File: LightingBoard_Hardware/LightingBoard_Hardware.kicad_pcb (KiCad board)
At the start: 2 copper layers, 61 x 108.8 mm, 19 parts, among them U1 LDD-1500L, U2 LDD-1500L, U3 TM4C129E_Launchpad, U4 +5V OKI

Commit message: Fixed detached ground polygon
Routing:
- net GND: track 8.38 -> 17.5 mm, vias 2 -> 4
- net Headlight_OnOff_PWM1: track 111.4 -> 110.1 mm
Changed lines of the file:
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@@
     (thickness 1.6)
     (drawings 29)
-    (tracks 81)
+    (tracks 88)
     (zones 0)
     (modules 19)
@@
   )
   (setup
-    (last_trace_width 0.25)
+    (last_trace_width 1.27)
     (user_trace_width 0.0381)
     (user_trace_width 0.03998)
@@
   (segment (start 158.496 83.439) (end 155.956 83.439) (width 1.27) (layer F.Cu) (net 2))
   (segment (start 158.496 61.849) (end 155.956 61.849) (width 1.27) (layer F.Cu) (net 2))
+  (segment (start 155.956 61.849) (end 151.384 61.849) (width 1.27) (layer B.Cu) (net 2))
+  (segment (start 155.956 83.439) (end 151.384 83.439) (width 1.27) (layer B.Cu) (net 2))
+  (segment (start 151.384 61.849) (end 151.384 61.849) (width 1.27) (layer B.Cu) (net 2))
+  (via (at 151.384 61.849) (size 1.27) (drill 0.4) (layers F.Cu B.Cu) (net 2))
+  (segment (start 151.384 83.439) (end 151.384 83.439) (width 1.27) (layer B.Cu) (net 2))
+  (via (at 151.384 83.439) (size 1.27) (drill 0.4) (layers F.Cu B.Cu) (net 2))
   (segment (start 138.303 123.317) (end 138.303 119.634) (width 0.381) (layer F.Cu) (net 3))
   (segment (start 120.2944 112.775) (end 135.763 112.775) (width 0.762) (layer F.Cu) (net 3))
@@
   (segment (start 121.031 51.943) (end 121.031 47.879) (width 0.381) (layer B.Cu) (net 13))
   (segment (start 153.67 97.536) (end 153.67 97.536) (width 0.25) (layer F.Cu) (net 14))
-  (segment (start 151.416 80.296) (end 151.416 98.679) (width 0.381) (layer B.Cu) (net 14))
-  (segment (start 150.114 78.994) (end 151.416 80.296) (width 0.381) (layer B.Cu) (net 14))
-  (segment (start 121.7047 78.994) (end 150.114 78.994) (width 0.381) (layer B.Cu) (net 14))
   (segment (start 118.008001 74.903601) (end 118.008001 75.297301) (width 0.381) (layer B.Cu) (net 14))
   (segment (start 118.008001 75.297301) (end 121.7047 78.994) (width 0.381) (layer B.Cu) (net 14))
@@
   (segment (start 154.714 43.561) (end 153.67 44.605) (width 0.381) (layer F.Cu) (net 14))
   (segment (start 153.67 45.170685) (end 153.67 97.536) (width 0.381) (layer F.Cu) (net 14))
+  (segment (start 151.416 98.679) (end 149.225 96.488) (width 0.381) (layer B.Cu) (net 14))
+  (segment (start 149.225 96.488) (end 149.225 80.264) (width 0.381) (layer B.Cu) (net 14))
+  (segment (start 149.225 80.264) (end 147.955 78.994) (width 0.381) (layer B.Cu) (net 14))
+  (segment (start 147.955 78.994) (end 121.7047 78.994) (width 0.381) (layer B.Cu) (net 14))
   (segment (start 115.468001 74.903601) (end 115.468001 75.297301) (width 0.381) (layer B.Cu) (net 15))
   (segment (start 149.257 74.93) (end 151.416 77.089) (width 0.381) (layer B.Cu) (net 15))

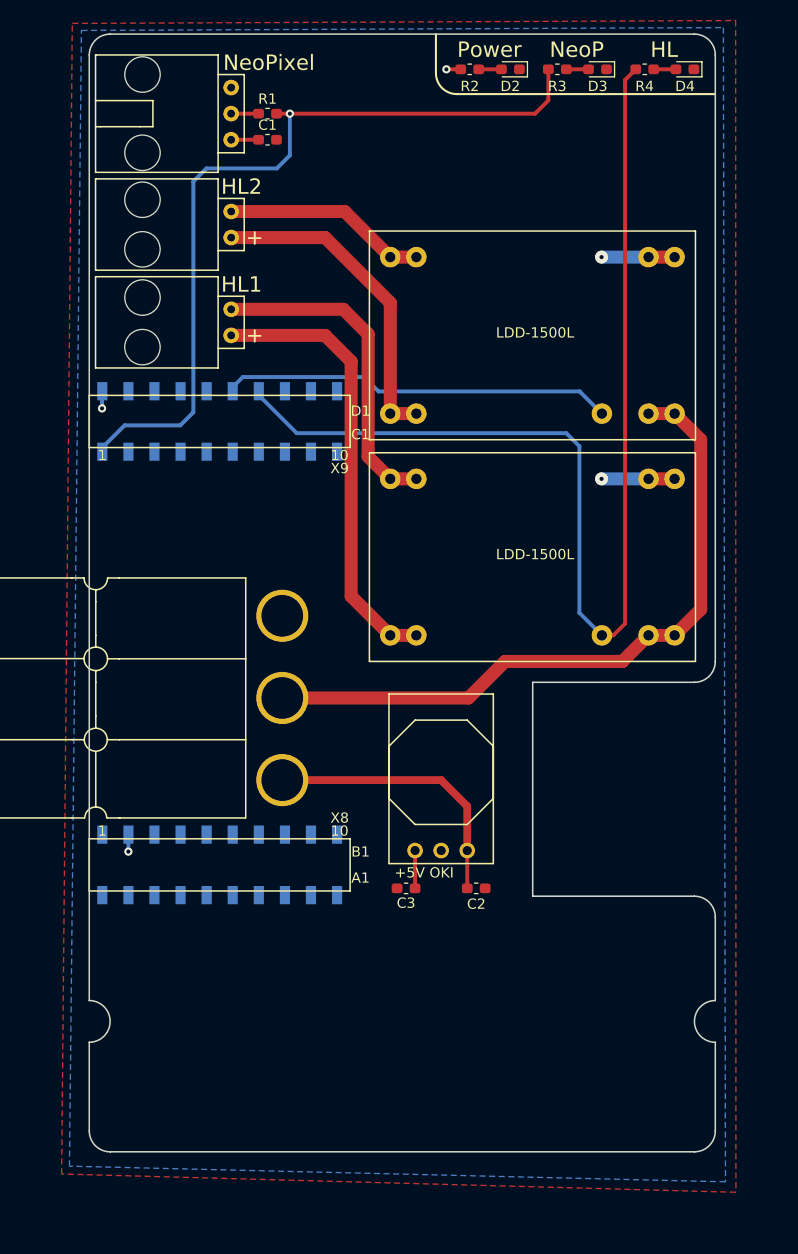
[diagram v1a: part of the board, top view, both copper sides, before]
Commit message: Traces probably finished
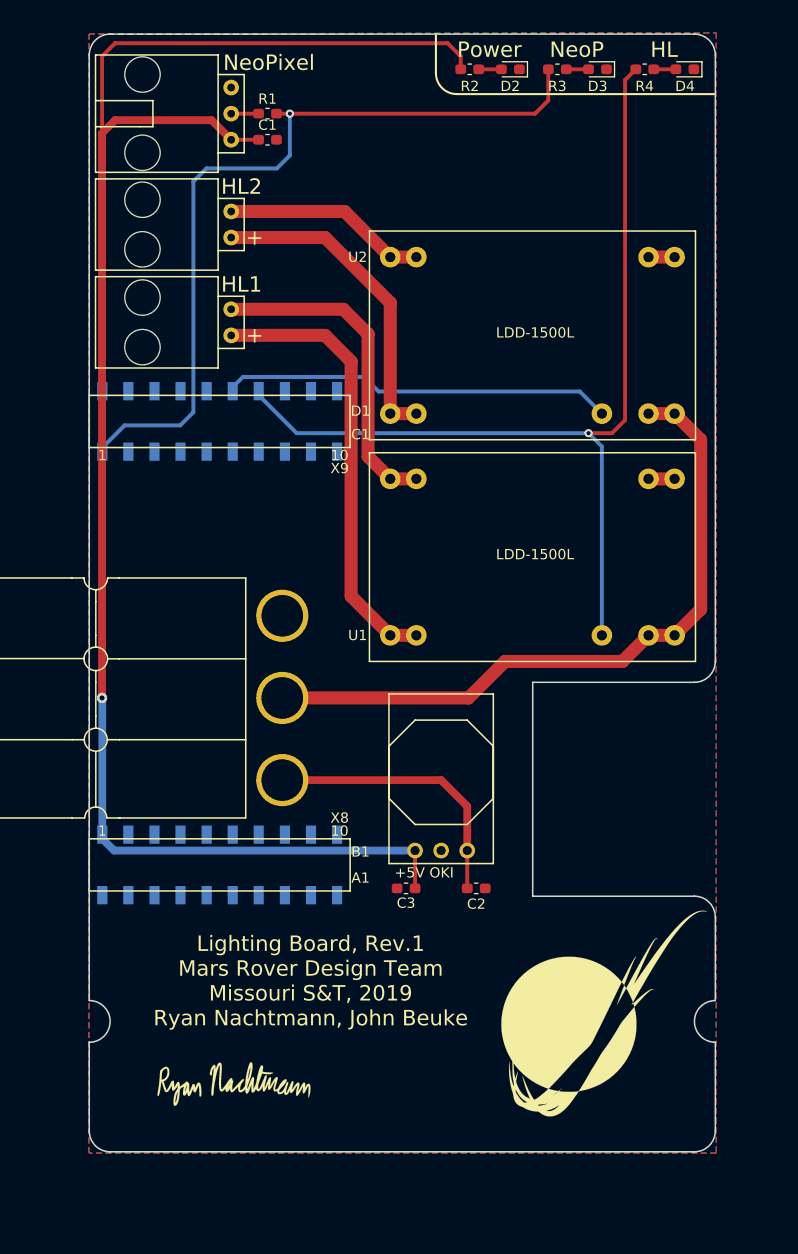
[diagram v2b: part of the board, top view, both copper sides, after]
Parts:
- added G***: LOGO, LightingBoard_Hardware2:Ryan Signature, F.Cu at (116.2, 142.7)
- added G***: LOGO, MRDT_Silkscreens:MRDT_Logo_20mm, F.Cu at (151.6, 135.5)
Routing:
- net +5V: track 7.75 -> 164.6 mm
- net Headlight_OnOff_PWM1: track 110.1 -> 92.9 mm, vias 0 -> 1
- net GND: track 17.5 -> 5.08 mm, vias 4 -> 0
- added copper zone on B.Cu, net GND
- removed copper zone on B.Cu, net +5V
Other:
- board text added: "Lighting Board, Rev.1 Mars Rover Design Team Missouri S&T, 2019 Ryan Nachtmann, John Beuke"

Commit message: Probably finished the traces 2.0
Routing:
- net +5V: vias 1 -> 2
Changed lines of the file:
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@@
     (thickness 1.6)
     (drawings 30)
-    (tracks 89)
+    (tracks 91)
     (zones 0)
     (modules 21)
@@
   )
   (setup
-    (last_trace_width 0.25)
+    (last_trace_width 0.762)
     (user_trace_width 0.0381)
     (user_trace_width 0.03998)
@@
   (segment (start 102.768001 104.800001) (end 102.743 104.775) (width 0.762) (layer B.Cu) (net 1))
   (segment (start 102.743 104.775) (end 102.743 49.784) (width 0.762) (layer F.Cu) (net 1))
-  (segment (start 102.743 49.784) (end 104.013 48.514) (width 0.762) (layer F.Cu) (net 1))
-  (segment (start 104.013 48.514) (end 104.013 48.514) (width 0.762) (layer F.Cu) (net 1))
-  (segment (start 115.316 50.419) (end 113.411 48.514) (width 0.762) (layer F.Cu) (net 1))
-  (segment (start 113.411 48.514) (end 104.013 48.514) (width 0.762) (layer F.Cu) (net 1))
   (segment (start 102.743 49.784) (end 102.743 42.291) (width 0.381) (layer F.Cu) (net 1))
   (segment (start 102.743 42.291) (end 104.013 41.021) (width 0.381) (layer F.Cu) (net 1))
@@
   (segment (start 136.398 41.021) (end 137.668 42.291) (width 0.381) (layer F.Cu) (net 1))
   (segment (start 137.668 42.291) (end 137.668 43.561) (width 0.381) (layer F.Cu) (net 1))
+  (segment (start 102.743 49.784) (end 102.743 49.784) (width 0.762) (layer F.Cu) (net 1))
+  (via (at 102.743 49.784) (size 1) (drill 0.5) (layers F.Cu B.Cu) (net 1))
+  (segment (start 102.743 49.784) (end 104.013 48.514) (width 0.762) (layer B.Cu) (net 1))
+  (segment (start 115.316 50.419) (end 113.411 48.514) (width 0.762) (layer B.Cu) (net 1))
+  (segment (start 113.411 48.514) (end 104.013 48.514) (width 0.762) (layer B.Cu) (net 1))
   (segment (start 158.496 83.439) (end 155.956 83.439) (width 1.27) (layer F.Cu) (net 2))
   (segment (start 158.496 61.849) (end 155.956 61.849) (width 1.27) (layer F.Cu) (net 2))
@@
   (segment (start 153.67 44.605) (end 153.67 44.605) (width 0.25) (layer F.Cu) (net 14))
   (segment (start 154.714 43.561) (end 153.67 44.605) (width 0.381) (layer F.Cu) (net 14))
-  (segment (start 151.416 98.679) (end 151.416 80.296) (width 0.381) (layer B.Cu) (net 14))
-  (segment (start 151.416 80.296) (end 150.114 78.994) (width 0.381) (layer B.Cu) (net 14))
   (segment (start 150.114 78.994) (end 121.7047 78.994) (width 0.381) (layer B.Cu) (net 14))
   (segment (start 151.416 80.296) (end 151.416 80.296) (width 0.381) (layer B.Cu) (net 14))
   (segment (start 150.114 78.994) (end 150.114 78.994) (width 0.381) (layer B.Cu) (net 14))
-  (via (at 150.114 78.994) (size 0.8) (drill 0.4) (layers F.Cu B.Cu) (net 14))
-  (segment (start 150.114 78.994) (end 152.4 78.994) (width 0.381) (layer F.Cu) (net 14))
-  (segment (start 152.4 78.994) (end 153.67 77.724) (width 0.381) (layer F.Cu) (net 14))
-  (segment (start 153.67 77.724) (end 153.67 44.605) (width 0.381) (layer F.Cu) (net 14))
+  (segment (start 153.67 44.605) (end 153.67 44.605) (width 0.25) (layer F.Cu) (net 14))
+  (via (at 153.67 44.605) (size 0.8) (drill 0.4) (layers F.Cu B.Cu) (net 14))
+  (segment (start 153.67 44.605) (end 153.67 77.724) (width 0.381) (layer B.Cu) (net 14))
+  (segment (start 153.67 77.724) (end 152.4 78.994) (width 0.381) (layer B.Cu) (net 14))
+  (segment (start 152.4 78.994) (end 150.114 78.994) (width 0.381) (layer B.Cu) (net 14))
+  (segment (start 151.416 98.679) (end 151.416 80.296) (width 0.381) (layer B.Cu) (net 14))
+  (segment (start 151.416 80.296) (end 150.114 78.994) (width 0.381) (layer B.Cu) (net 14))
   (segment (start 115.468001 74.903601) (end 115.468001 75.297301) (width 0.381) (layer B.Cu) (net 15))
   (segment (start 149.257 74.93) (end 151.416 77.089) (width 0.381) (layer B.Cu) (net 15))

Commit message: Added John's Signature
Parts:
- added G***: LOGO, LightingBoard_Hardware2:John Signature, F.Cu at (133.6, 143.3)

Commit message: Final Board
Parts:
- moved Conn2 0.64 mm to (114.7, 68.2)
- moved Conn3 0.64 mm to (114.7, 58.7)
- moved Conn4 0.64 mm to (114.7, 47.9)
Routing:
- net /Headlight_V2-: track 19.9 -> 23.8 mm
- net /Headlight_V2+: track 31.5 -> 33.6 mm
- net /Headlight_V1+: track 43.5 -> 44.6 mm
- net /Headlight_V1-: track 31.9 -> 32.9 mm
- net Net-(Conn4-Pad2): track 2.67 -> 3.30 mm
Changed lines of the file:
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@@
     (thickness 1.6)
     (drawings 30)
-    (tracks 91)
+    (tracks 99)
     (zones 0)
     (modules 22)
@@
   )
   (setup
-    (last_trace_width 0.25)
+    (last_trace_width 1.905)
     (user_trace_width 0.0381)
     (user_trace_width 0.03998)
@@
     (user_trace_width 0.762)
     (user_trace_width 1.27)
+    (user_trace_width 1.905)
     (trace_clearance 0.2)
     (zone_clearance 0.508)
@@
     (solder_mask_min_width 0.25)
     (aux_axis_origin 0 0)
-    (visible_elements 7FFFFFFF)
+    (visible_elements 7FFFEFFF)
     (pcbplotparams
       (layerselection 0x010fc_ffffffff)
@@
   )
   (module MRDT_Connectors:MOLEX_SL_02_Horizontal (layer F.Cu)
-    (at 115.316 68.199 90)
+    (at 114.681 68.199 90)
     (fp_text reference Conn2 (at 0 2.54 90) (layer F.SilkS) hide
       (effects (font (size 1 1) (thickness 0.15)))
@@
   )
   (module MRDT_Connectors:MOLEX_SL_02_Horizontal (layer F.Cu)
-    (at 115.316 58.674 90)
+    (at 114.681 58.674 90)
     (fp_text reference Conn3 (at 0 2.54 90) (layer F.SilkS) hide
       (effects (font (size 1 1) (thickness 0.15)))
@@
   )
   (module MRDT_Connectors:MOLEX_SL_03_Horizontal (layer F.Cu)
-    (at 115.316 47.879 90)
+    (at 114.681 47.879 90)
     (fp_text reference Conn4 (at -1.27 2.54 90) (layer F.SilkS) hide
       (effects (font (size 1 1) (thickness 0.15)))
@@
   (gr_arc (start 101.4984 136.271) (end 101.4984 138.303) (angle -180) (layer Edge.Cuts) (width 0.15))
   (segment (start 133.223 119.634) (end 133.223 123.317) (width 0.381) (layer F.Cu) (net 1))
-  (segment (start 117.983 50.419) (end 115.316 50.419) (width 0.381) (layer F.Cu) (net 1))
   (segment (start 102.768001 118.477301) (end 102.768001 118.083601) (width 0.762) (layer B.Cu) (net 1))
   (segment (start 102.768001 118.477301) (end 103.9247 119.634) (width 0.762) (layer B.Cu) (net 1))
@@
   (via (at 102.743 49.784) (size 1) (drill 0.5) (layers F.Cu B.Cu) (net 1))
   (segment (start 102.743 49.784) (end 104.013 48.514) (width 0.762) (layer B.Cu) (net 1))
-  (segment (start 115.316 50.419) (end 113.411 48.514) (width 0.762) (layer B.Cu) (net 1))
-  (segment (start 113.411 48.514) (end 104.013 48.514) (width 0.762) (layer B.Cu) (net 1))
+  (segment (start 114.681 50.419) (end 112.776 48.514) (width 0.762) (layer B.Cu) (net 1))
+  (segment (start 112.776 48.514) (end 104.013 48.514) (width 0.762) (layer B.Cu) (net 1))
+  (segment (start 117.983 50.419) (end 114.681 50.419) (width 0.381) (layer F.Cu) (net 1))
   (segment (start 158.496 83.439) (end 155.956 83.439) (width 1.27) (layer F.Cu) (net 2))
   (segment (start 158.496 61.849) (end 155.956 61.849) (width 1.27) (layer F.Cu) (net 2))
@@
   (segment (start 135.763 112.776) (end 138.303 115.316) (width 0.762) (layer F.Cu) (net 3))
   (segment (start 138.303 115.316) (end 138.303 119.634) (width 0.762) (layer F.Cu) (net 3))
-  (segment (start 158.496 98.679) (end 155.956 98.679) (width 1.27) (layer F.Cu) (net 4))
-  (segment (start 158.496 77.089) (end 155.956 77.089) (width 1.27) (layer F.Cu) (net 4))
-  (segment (start 120.2944 104.776) (end 138.429 104.776) (width 1.27) (layer F.Cu) (net 4))
-  (segment (start 138.429 104.776) (end 141.986 101.219) (width 1.27) (layer F.Cu) (net 4))
-  (segment (start 141.986 101.219) (end 153.416 101.219) (width 1.27) (layer F.Cu) (net 4))
-  (segment (start 153.416 101.219) (end 155.956 98.679) (width 1.27) (layer F.Cu) (net 4))
-  (segment (start 158.496 98.679) (end 161.036 96.139) (width 1.27) (layer F.Cu) (net 4))
-  (segment (start 161.036 96.139) (end 161.036 79.629) (width 1.27) (layer F.Cu) (net 4))
-  (segment (start 161.036 79.629) (end 158.496 77.089) (width 1.27) (layer F.Cu) (net 4))
-  (segment (start 133.35 98.679) (end 130.81 98.679) (width 1.27) (layer F.Cu) (net 5))
-  (segment (start 130.81 98.679) (end 127 94.869) (width 1.27) (layer F.Cu) (net 5))
-  (segment (start 127 94.869) (end 127 72.009) (width 1.27) (layer F.Cu) (net 5))
-  (segment (start 127 72.009) (end 124.46 69.469) (width 1.27) (layer F.Cu) (net 5))
-  (segment (start 124.46 69.469) (end 115.316 69.469) (width 1.27) (layer F.Cu) (net 5))
-  (segment (start 133.35 83.439) (end 130.81 83.439) (width 1.27) (layer F.Cu) (net 6))
-  (segment (start 126.238 66.929) (end 115.316 66.929) (width 1.27) (layer F.Cu) (net 6))
-  (segment (start 128.651 69.342) (end 126.238 66.929) (width 1.27) (layer F.Cu) (net 6))
-  (segment (start 130.81 83.439) (end 128.651 81.28) (width 1.27) (layer F.Cu) (net 6))
-  (segment (start 128.651 81.28) (end 128.651 69.342) (width 1.27) (layer F.Cu) (net 6))
-  (segment (start 133.35 61.849) (end 130.81 61.849) (width 1.27) (layer F.Cu) (net 7))
-  (segment (start 130.81 61.849) (end 126.365 57.404) (width 1.27) (layer F.Cu) (net 7))
-  (segment (start 126.365 57.404) (end 115.316 57.404) (width 1.27) (layer F.Cu) (net 7))
-  (segment (start 133.35 77.089) (end 130.81 77.089) (width 1.27) (layer F.Cu) (net 8))
-  (segment (start 130.81 77.089) (end 130.81 66.294) (width 1.27) (layer F.Cu) (net 8))
-  (segment (start 130.81 66.294) (end 124.46 59.944) (width 1.27) (layer F.Cu) (net 8))
-  (segment (start 124.46 59.944) (end 115.316 59.944) (width 1.27) (layer F.Cu) (net 8))
-  (segment (start 117.983 47.879) (end 115.316 47.879) (width 0.381) (layer F.Cu) (net 9))
+  (segment (start 120.2944 104.776) (end 138.429 104.776) (width 1.905) (layer F.Cu) (net 4))
+  (segment (start 138.429 104.776) (end 141.986 101.219) (width 1.905) (layer F.Cu) (net 4))
+  (segment (start 141.986 101.219) (end 153.416 101.219) (width 1.905) (layer F.Cu) (net 4))
+  (segment (start 153.416 101.219) (end 155.956 98.679) (width 1.905) (layer F.Cu) (net 4))
+  (segment (start 155.956 98.679) (end 158.496 98.679) (width 1.905) (layer F.Cu) (net 4))
+  (segment (start 158.496 98.679) (end 161.036 96.139) (width 1.905) (layer F.Cu) (net 4))
+  (segment (start 161.036 96.139) (end 161.036 79.629) (width 1.905) (layer F.Cu) (net 4))
+  (segment (start 161.036 79.629) (end 158.496 77.089) (width 1.905) (layer F.Cu) (net 4))
+  (segment (start 158.496 77.089) (end 155.956 77.089) (width 1.905) (layer F.Cu) (net 4))
+  (segment (start 130.81 98.679) (end 125.73 93.599) (width 1.905) (layer F.Cu) (net 5))
+  (segment (start 125.73 93.599) (end 125.73 73.279) (width 1.905) (layer F.Cu) (net 5))
+  (segment (start 125.73 73.279) (end 121.92 69.469) (width 1.905) (layer F.Cu) (net 5))
+  (segment (start 130.81 98.679) (end 133.35 98.679) (width 1.905) (layer F.Cu) (net 5))
+  (segment (start 114.681 69.469) (end 117.221 69.469) (width 1.905) (layer F.Cu) (net 5))
+  (segment (start 121.92 69.469) (end 117.221 69.469) (width 1.905) (layer F.Cu) (net 5))
+  (segment (start 117.221 69.469) (end 115.316 69.469) (width 1.905) (layer F.Cu) (net 5))
+  (segment (start 130.81 83.439) (end 133.35 83.439) (width 1.905) (layer F.Cu) (net 6))
+  (segment (start 128.27 80.899) (end 130.81 83.439) (width 1.905) (layer F.Cu) (net 6))
+  (segment (start 128.27 72.009) (end 128.27 80.899) (width 1.905) (layer F.Cu) (net 6))
+  (segment (start 123.19 66.929) (end 128.27 72.009) (width 1.905) (layer F.Cu) (net 6))
+  (segment (start 114.681 66.929) (end 117.475 66.929) (width 1.905) (layer F.Cu) (net 6))
+  (segment (start 115.316 66.929) (end 117.475 66.929) (width 1.905) (layer F.Cu) (net 6))
+  (segment (start 117.475 66.929) (end 123.19 66.929) (width 1.905) (layer F.Cu) (net 6))
+  (segment (start 133.35 61.849) (end 130.81 61.849) (width 1.905) (layer F.Cu) (net 7))
+  (segment (start 130.81 61.849) (end 126.365 57.404) (width 1.905) (layer F.Cu) (net 7))
+  (segment (start 114.681 57.404) (end 118.618 57.404) (width 1.905) (layer F.Cu) (net 7))
+  (segment (start 126.365 57.404) (end 118.618 57.404) (width 1.905) (layer F.Cu) (net 7))
+  (segment (start 118.618 57.404) (end 115.316 57.404) (width 1.905) (layer F.Cu) (net 7))
+  (segment (start 133.35 77.089) (end 130.81 77.089) (width 1.905) (layer F.Cu) (net 8))
+  (segment (start 130.81 77.089) (end 130.81 66.294) (width 1.905) (layer F.Cu) (net 8))
+  (segment (start 130.81 66.294) (end 124.46 59.944) (width 1.905) (layer F.Cu) (net 8))
+  (segment (start 114.681 59.944) (end 116.84 59.944) (width 1.905) (layer F.Cu) (net 8))
+  (segment (start 124.46 59.944) (end 116.84 59.944) (width 1.905) (layer F.Cu) (net 8))
+  (segment (start 116.84 59.944) (end 115.316 59.944) (width 1.905) (layer F.Cu) (net 8))
+  (segment (start 117.983 47.879) (end 114.681 47.879) (width 0.381) (layer F.Cu) (net 9))
   (segment (start 139.418 43.561) (end 141.633 43.561) (width 0.381) (layer F.Cu) (net 10))
   (segment (start 147.955 43.561) (end 150.114 43.561) (width 0.381) (layer F.Cu) (net 11))

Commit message: Added Gerbs
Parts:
- added G***: LOGO, MRDT_Silkscreens:Nothing_3mm_Cu, B.Cu at (147.2, 134.1)
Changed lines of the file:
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@@
     (tracks 99)
     (zones 0)
-    (modules 22)
+    (modules 23)
     (nets 50)
   )
@@
   )
   (setup
-    (last_trace_width 1.905)
+    (last_trace_width 0.25)
     (user_trace_width 0.0381)
     (user_trace_width 0.03998)
@@
       (outputformat 1)
       (mirror false)
-      (drillshape 1)
+      (drillshape 0)
       (scaleselection 1)
-      (outputdirectory ""))
+      (outputdirectory "Gerbs/"))
   )
   (net 0 "")
@@
       (xy -6.431895 -2.508434)) (layer F.SilkS) (width 0.01))
   )
+  (module MRDT_Silkscreens:Nothing_3mm_Cu (layer B.Cu)
+    (at 147.193 134.112 180)
+    (fp_text reference G*** (at -1.2954 2.64668 180) (layer B.SilkS) hide
+      (effects (font (size 1.524 1.524) (thickness 0.3)) (justify mirror))
+    )
+    (fp_text value LOGO (at -1.016 6.604 180) (layer F.SilkS) hide
+      (effects (font (size 1.524 1.524) (thickness 0.3)))
+    )
+    (fp_line (start -1.15316 -1.91008) (end 0 0.05588) (layer B.Cu) (width 0.15))
+    (fp_line (start 0 0.05588) (end 1.09728 -1.8796) (layer B.Cu) (width 0.15))
+    (fp_line (start 1.09728 -1.8796) (end -1.143 -1.89992) (layer B.Cu) (width 0.15))
+    (fp_circle (center -0.0254 -1.23952) (end 0.06604 -1.48336) (layer B.Cu) (width 0.15))
+    (fp_arc (start -0.02032 -1.9304) (end -0.75184 -1.23952) (angle -93.2) (layer B.Cu) (width 0.15))
+    (fp_arc (start -0.00508 -0.51308) (end 0.70104 -1.22936) (angle -88) (layer B.Cu) (width 0.15))
+  )
   (gr_text "Lighting Board, Rev.1\nMars Rover Design Team\nMissouri S&T, 2019\nRyan Nachtmann, John Beuke" (at 123.063 132.334) (layer F.SilkS)
